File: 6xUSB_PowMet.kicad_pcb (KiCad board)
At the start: 2 copper layers, 56 parts, among them IC1 ATMEGA32-M, P1 USB_A, P2 USB_A, P3 USB_A, P4 USB_A, P5 USB_A, P6 USB_A, P7 CONN_01X08, P8 CONN_01X03, P9 CONN_01X02, U1 LM1117MP-2.5, U2 LT6106, U3 LT6106, U4 LT6106, U5 LT6106, U6 LT6106, U7 LT6106

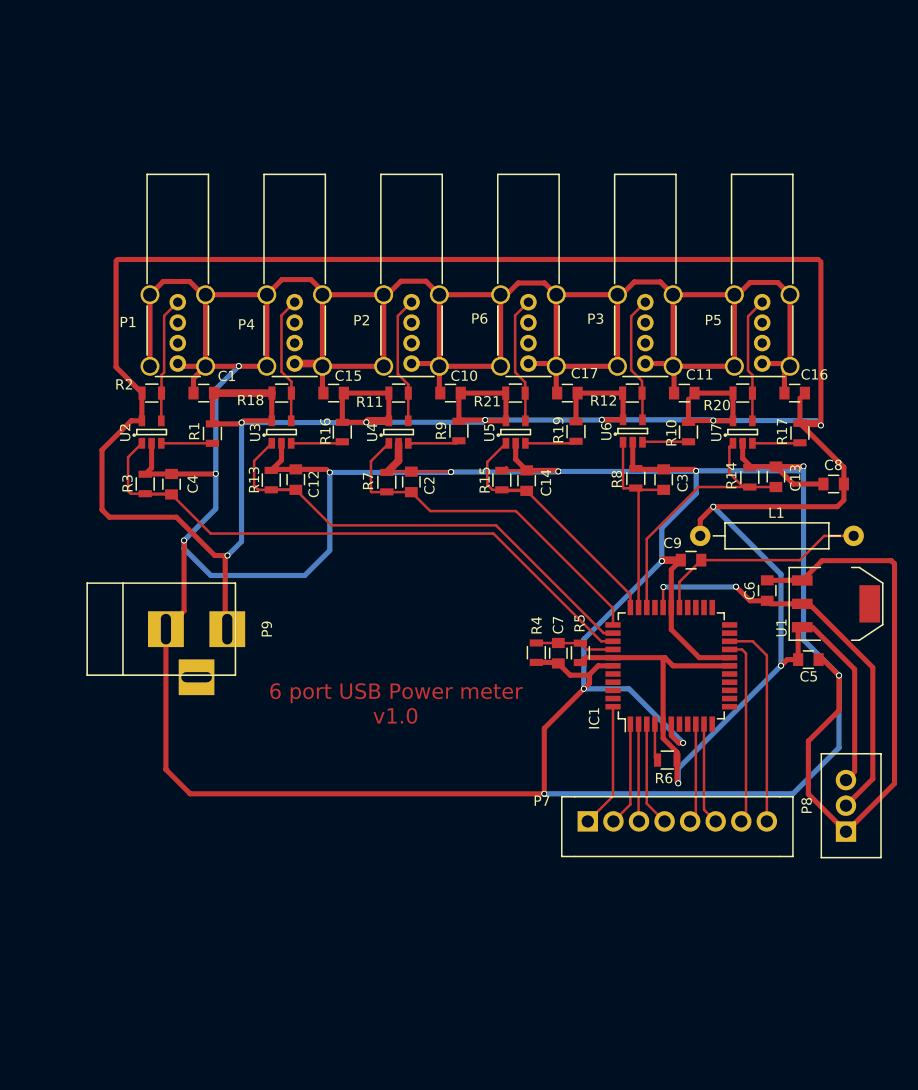
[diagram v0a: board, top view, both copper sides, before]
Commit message: Schematic updates
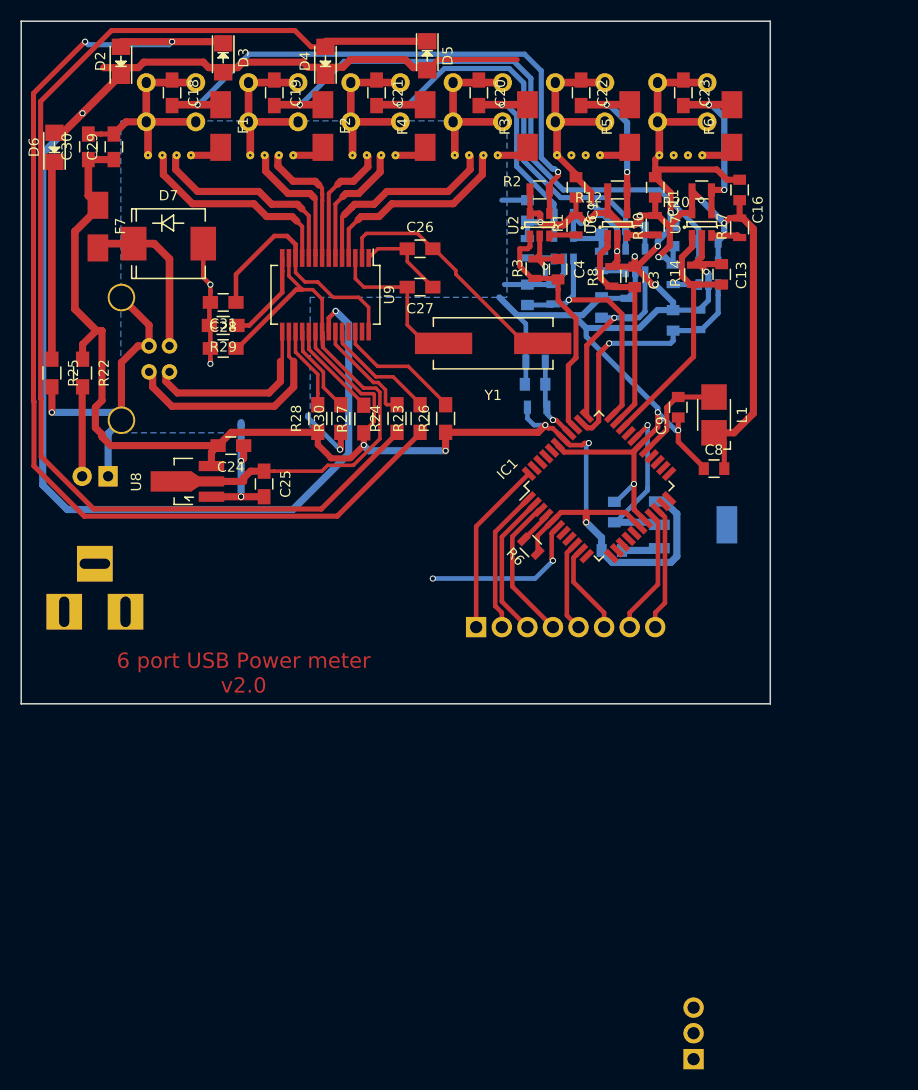
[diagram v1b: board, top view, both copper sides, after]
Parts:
- added C18: 10uF, Capacitors_SMD:C_0805_HandSoldering, F.Cu at (110.0, 55.5)
- added C19: 10uF, Capacitors_SMD:C_0805_HandSoldering, F.Cu at (120.0, 55.5)
- added C20: 10uF, Capacitors_SMD:C_0805_HandSoldering, F.Cu at (140.0, 55.5)
- added C21: 10uF, Capacitors_SMD:C_0805_HandSoldering, F.Cu at (130.0, 55.5)
- added C22: 10uF, Capacitors_SMD:C_0805_HandSoldering, F.Cu at (150.0, 55.5)
- added C23: 10uF, Capacitors_SMD:C_0805_HandSoldering, F.Cu at (160.0, 55.5)
- added C24: 4.7uF, Capacitors_SMD:C_0805_HandSoldering, F.Cu at (115.8, 90.0)
- added C25: 4.7uF, Capacitors_SMD:C_0805_HandSoldering, F.Cu at (119.0, 93.8)
- added C26: 10pF, Capacitors_SMD:C_0805_HandSoldering, F.Cu at (134.2, 70.8)
- added C27: 10pF, Capacitors_SMD:C_0805_HandSoldering, F.Cu at (134.2, 74.5)
- added C28: 10uF, Capacitors_SMD:C_0805_HandSoldering, F.Cu at (115.0, 80.5)
- added C29: 10nF, Capacitors_SMD:C_0805_HandSoldering, F.Cu at (104.3, 60.8)
- added C30: 10uF, Capacitors_SMD:C_0805_HandSoldering, F.Cu at (101.8, 60.8)
- added C31: 10uF, Capacitors_SMD:C_0805_HandSoldering, F.Cu at (115.0, 76.0)
- added D1: Power, LEDs:LED-5MM, B.Cu at (103.8, 93.0)
- added D2: Led_Small, LEDs:LED_1206, F.Cu at (105.0, 52.4)
- added D3: Led_Small, LEDs:LED_1206, F.Cu at (115.0, 52.1)
- added D4: Led_Small, LEDs:LED_1206, F.Cu at (125.0, 52.4)
- added D5: Led_Small, LEDs:LED_1206, F.Cu at (135.0, 51.9)
- added D6: Led_Small, LEDs:LED_1206, F.Cu at (98.5, 60.8)
- added D7: 5.1V, Diodes_SMD:SMC_Standard, F.Cu at (109.7, 70.2)
- added F1: F_Small, Fuse_Holders_and_Fuses:Fuse_SMD1206_HandSoldering, F.Cu at (114.8, 58.8)
- added F2: F_Small, Fuse_Holders_and_Fuses:Fuse_SMD1206_HandSoldering, F.Cu at (124.8, 58.8)
- added F3: F_Small, Fuse_Holders_and_Fuses:Fuse_SMD1206_HandSoldering, F.Cu at (144.8, 58.8)
- added F4: F_Small, Fuse_Holders_and_Fuses:Fuse_SMD1206_HandSoldering, F.Cu at (134.8, 58.8)
- added F5: F_Small, Fuse_Holders_and_Fuses:Fuse_SMD1206_HandSoldering, F.Cu at (154.8, 58.8)
- added F6: F_Small, Fuse_Holders_and_Fuses:Fuse_SMD1206_HandSoldering, F.Cu at (164.8, 58.8)
- added F7: F_Small, Fuse_Holders_and_Fuses:Fuse_SMD1206_HandSoldering, F.Cu at (102.8, 68.6)
- added P10: USB_B, Connect:USB_B, B.Cu at (109.7, 80.2)
- added R22: 330, Resistors_SMD:R_0805_HandSoldering, F.Cu at (101.2, 82.9)
- added R23: 330, Resistors_SMD:R_0805_HandSoldering, F.Cu at (134.2, 87.3)
- added R24: 330, Resistors_SMD:R_0805_HandSoldering, F.Cu at (132.0, 87.3)
- added R25: 330, Resistors_SMD:R_0805_HandSoldering, F.Cu at (98.2, 82.9)
- added R26: 10K, Resistors_SMD:R_0805_HandSoldering, F.Cu at (136.8, 87.3)
- added R27: 10K, Resistors_SMD:R_0805_HandSoldering, F.Cu at (128.8, 87.4)
- added R28: 10K, Resistors_SMD:R_0805_HandSoldering, F.Cu at (124.2, 87.3)
- added R29: 2.7K, Resistors_SMD:R_0805_HandSoldering, F.Cu at (115.0, 78.2)
- added R30: 10K, Resistors_SMD:R_0805_HandSoldering, F.Cu at (126.5, 87.3)
- added U8: AP1117E33, TO_SOT_Packages_SMD:SOT89-3_Housing_Handsoldering, F.Cu at (111.5, 93.5)
- added U9: FE1.1s, Housings_SSOP:SSOP-28_5.3x10.2mm_Pitch0.65mm, F.Cu at (125.0, 75.2)
- added Y1: 12Mhz, Crystals:Crystal_HC49-SD_SMD, F.Cu at (141.4, 80.0)
- C10, C12, C14, C15, C17, C2, C5, C6, C7, P7, P8, P9, R11, R13, R15, R16, R18, R19, R21, R4, R5, R7, R9, U1, U3, U4, U5: moved to B.Cu
- L1: footprint Resistors_ThroughHole:Resistor_Horizontal_RM15mm -> Inductors:Inductor_1212
- P1, P2, P3, P4, P5, P6: footprint Connect:USB_A_Vertical -> USB-A_vertical1:USB_A_Vertical; moved to B.Cu
- moved R13 44.6 mm to (161.5, 77.7)
- moved U3 44.5 mm to (162.4, 73.2)
- moved R18 44.3 mm to (162.4, 70.0), turned to 180 degrees
- moved R3 43.6 mm to (145.5, 72.7)
- moved C4 43.3 mm to (147.8, 72.8)
- moved U2 43.0 mm to (145.9, 68.4)
- moved R2 42.8 mm to (145.9, 65.0)
- moved C1 41.6 mm to (149.5, 64.8), turned to 270 degrees
- moved R1 41.0 mm to (149.5, 68.5)
- moved C12 40.1 mm to (159.0, 77.8)
- moved C15 36.6 mm to (159.0, 69.5), turned to 270 degrees
- moved R16 35.8 mm to (159.0, 73.3)
- moved R7 29.0 mm to (154.5, 76.5)
- moved U4 28.6 mm to (155.3, 71.9)
- moved R4 28.5 mm to (145.6, 81.8), turned to 0 degrees
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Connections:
- P1 pad 1: Net-(P1-Pad1) -> Net-(F1-Pad2)
- P1 pad 2: Net-(P1-Pad2) -> D1-
- P1 pad 3: Net-(P1-Pad3) -> D1+
- P2 pad 1: Net-(P2-Pad1) -> Net-(F4-Pad1)
- P2 pad 2: Net-(P2-Pad2) -> D3-
- P2 pad 3: Net-(P2-Pad3) -> D3+
- P3 pad 1: Net-(P3-Pad1) -> Net-(F5-Pad1)
- P4 pad 1: Net-(P4-Pad1) -> Net-(F2-Pad2)
- P4 pad 2: Net-(P4-Pad2) -> D2-
- P4 pad 3: Net-(P4-Pad3) -> D2+
- P5 pad 1: Net-(P5-Pad1) -> Net-(F6-Pad1)
- P6 pad 1: Net-(P6-Pad1) -> Net-(F3-Pad1)
- P6 pad 2: Net-(P6-Pad2) -> D4-
- P6 pad 3: Net-(P6-Pad3) -> D4+
- R11 pad 2: Net-(P2-Pad1) -> Net-(C21-Pad2)
- R12 pad 2: Net-(P3-Pad1) -> Net-(C22-Pad2)
- R18 pad 2: Net-(P4-Pad1) -> Net-(C19-Pad2)
- R2 pad 2: Net-(P1-Pad1) -> Net-(C18-Pad2)
- R20 pad 2: Net-(P5-Pad1) -> Net-(C23-Pad2)
- R21 pad 2: Net-(P6-Pad1) -> Net-(C20-Pad2)
- U2 pad 4: Net-(P1-Pad1) -> Net-(C18-Pad2)
- U3 pad 4: Net-(P4-Pad1) -> Net-(C19-Pad2)
- U4 pad 4: Net-(P2-Pad1) -> Net-(C21-Pad2)
- U5 pad 4: Net-(P6-Pad1) -> Net-(C20-Pad2)
- U6 pad 4: Net-(P3-Pad1) -> Net-(C22-Pad2)
- U7 pad 4: Net-(P5-Pad1) -> Net-(C23-Pad2)
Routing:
- net GND: track 650.9 -> 352.0 mm, vias 13 -> 20
- net +5V: track 399.0 -> 258.6 mm, vias 10 -> 11
- net Net-(D2-Pad1): track 0.00 -> 138.1 mm, vias 0 -> 2
- net Net-(D4-Pad2): track 0.00 -> 116.2 mm
- net Net-(D2-Pad2): track 0.00 -> 105.6 mm, vias 0 -> 2
- net Net-(C19-Pad2): track 0.00 -> 60.1 mm, vias 0 -> 1
- net Net-(C18-Pad2): track 0.00 -> 55.1 mm, vias 0 -> 2
- net /USB hub/3V3: track 0.00 -> 53.0 mm
- net Net-(C21-Pad2): track 0.00 -> 42.1 mm, vias 0 -> 1
- net Net-(C4-Pad2): track 62.1 -> 23.9 mm
- net Net-(C26-Pad2): track 0.00 -> 24.5 mm
- net /USB hub/1V8: track 0.00 -> 24.2 mm
- net Net-(C12-Pad2): track 48.7 -> 25.6 mm, vias 0 -> 1
- net +2.5V: track 40.4 -> 17.3 mm, vias 2 -> 1
- net D5+: track 0.00 -> 22.6 mm
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- added copper zone on B.Cu, net GND
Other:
- board outline added: 73.2 x 66.8 mm
- net class 2 added: clearance 0.25, trace_width 0.7, via_dia 0.6, via_drill 0.4
- board text added: "6 port USB Power meter v2.0"
- board text removed: "6 port USB Power meter v1.0"

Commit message: Schematic updates
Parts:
- removed P9: CONN_01X02, Connect:BARREL_JACK
- added C32: 47uF, Capacitors_SMD:C_1206_HandSoldering, B.Cu at (108.2, 111.5)
- added C33: 47uF, Capacitors_SMD:C_1206_HandSoldering, B.Cu at (111.0, 111.5)
- added C34: 10n, Capacitors_SMD:C_0805_HandSoldering, B.Cu at (117.2, 106.5)
- added C35: 180uF, Capacitors_SMD:c_elec_8x10.5, B.Cu at (130.5, 102.8)
- added C36: 100nF, Capacitors_SMD:C_0805_HandSoldering, F.Cu at (130.2, 111.5)
- added CON1: BARREL_JACK, Connect:JACK_ALIM, B.Cu at (97.8, 107.8)
- added D8: D_Schottky, Diodes_SMD:SMC_Handsoldering, B.Cu at (117.4, 101.2)
- added Q1: IRFR5305PBF, TO_SOT_Packages_SMD1:TO-252-2Lead, F.Cu at (120.3, 102.5)
- added R31: 10K, Resistors_SMD:R_0805_HandSoldering, B.Cu at (127.2, 111.4)
- added R32: 3.24K, Resistors_SMD:R_0805_HandSoldering, B.Cu at (123.8, 111.4)
- added R33: 470K, Resistors_SMD:R_0805_HandSoldering, F.Cu at (130.2, 105.6)
- added U10: TPS5450-EP_DDA_8, TPS5450-EP_DDA_8:DDA8_3X2P49, B.Cu at (117.2, 111.0)
- added U11: LTC4412, tom_kicad_lib:SOT-6, F.Cu at (125.5, 105.5)
- moved P8 41.6 mm to (164.5, 108.5)
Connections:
- D7 pad 1: +5V -> Net-(D7-Pad1)
- F7 pad 2: +5V -> Net-(D7-Pad1)
- P10 pad 1: +5V -> VREG
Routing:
- net GND: track 352.0 -> 486.2 mm, vias 20 -> 22
- net VREG: track 0.00 -> 70.8 mm, vias 0 -> 2
- net +5V: track 258.6 -> 305.5 mm, vias 11 -> 15
- net Net-(D2-Pad1): track 138.1 -> 178.5 mm
- net Net-(C32-Pad1): track 0.00 -> 13.0 mm
- net +2.5V: track 17.3 -> 29.7 mm, vias 1 -> 2
- net Net-(C34-Pad1): track 0.00 -> 11.7 mm
- net Net-(R31-Pad1): track 0.00 -> 7.52 mm
- net Net-(Q1-Pad1): track 0.00 -> 6.32 mm
- net Net-(R33-Pad2): track 0.00 -> 3.84 mm
- net Net-(D7-Pad1): track 0.00 -> 3.67 mm
- net Net-(C34-Pad2): track 0.00 -> 3.14 mm
